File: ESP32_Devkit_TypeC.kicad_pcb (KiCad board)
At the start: 2 copper layers, 25.3 x 48.2 mm, 43 parts, among them J1 USB_C_Receptacle_USB2.0, J2 Conn_01x19, J3 Conn_01x19, Q1 SS8050, Q2 SS8050, SW1 EN, SW2 BOOT, U1 MP2451, U2 CH340G, U3 ESP32-PICO-D4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

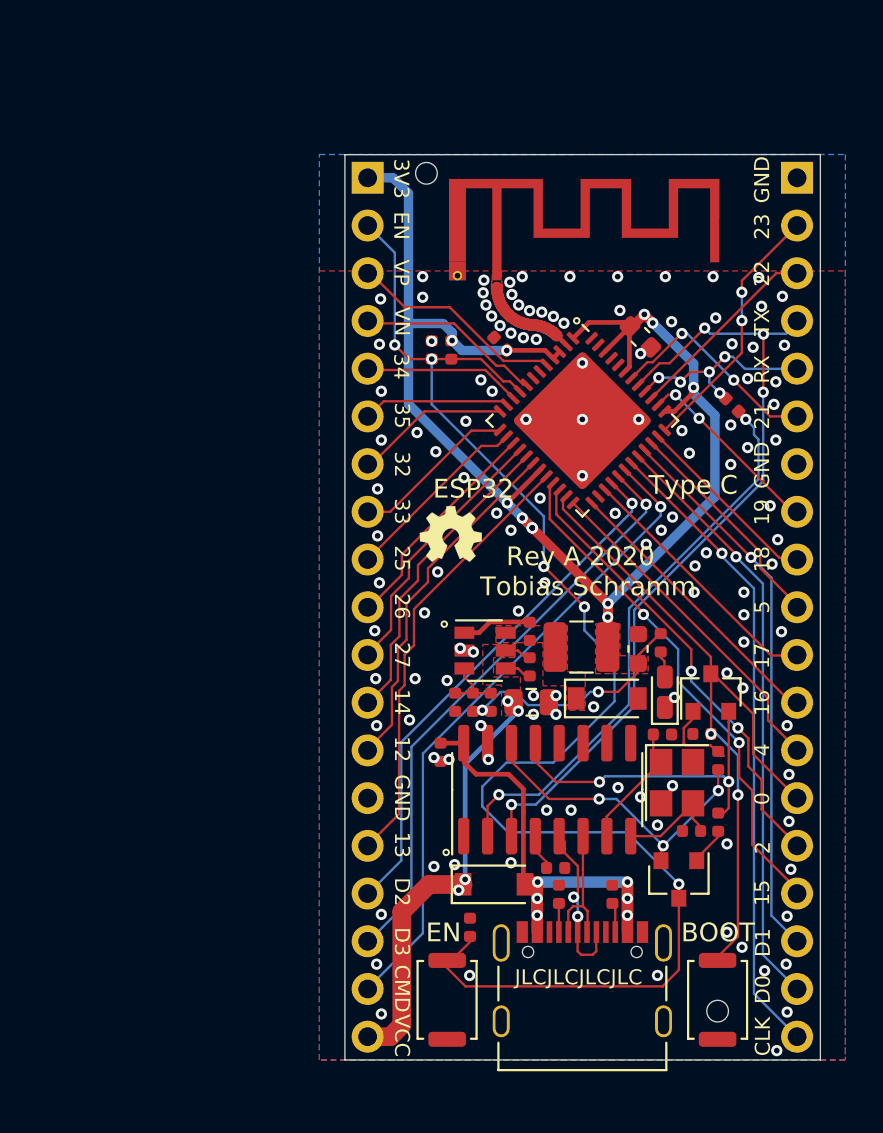
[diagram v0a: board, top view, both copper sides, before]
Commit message: Use ESP32 Pico D4 footprint
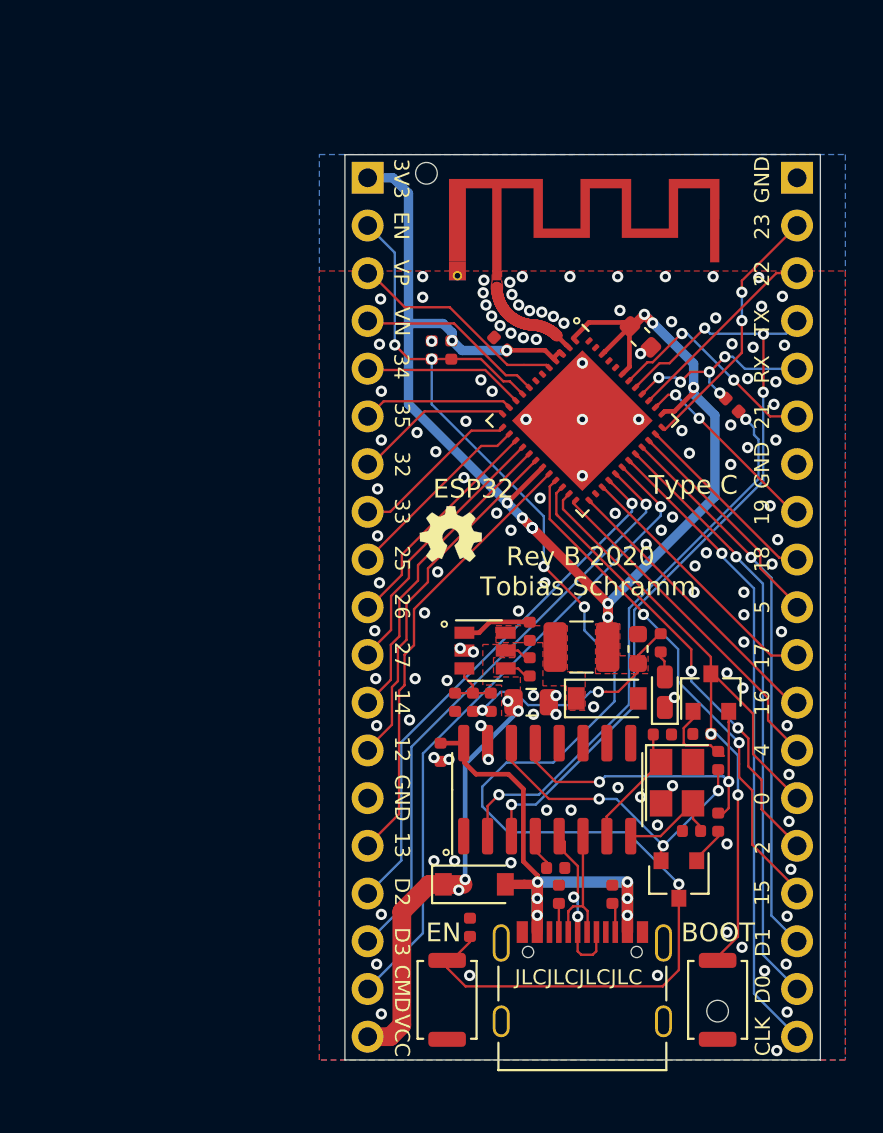
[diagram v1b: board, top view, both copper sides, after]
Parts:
- U3: footprint Package_DFN_QFN:QFN-48-1EP_7x7mm_P0.5mm_EP5.3x5.3mm -> Package_ESP32:ESP32-Pico-D4
- moved D1 1.05 mm to (94.2, 114.8)
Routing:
- net VBUS: track 25.2 -> 26.8 mm
- net +3V3: track 91.7 -> 92.9 mm
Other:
- board text added: "Rev B 2020"
- board text removed: "Rev A 2020"

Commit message: Rev B
Changes from Rev A:
 - Fix ESP32 Pico D4 footprint, now LGA
 - Add couple capacitor from EN to IO0
 - Add protection resistors to EN and IO0
 - Move VBUS diode for easier USB Type C jack assembly
 - Small routing optimizations
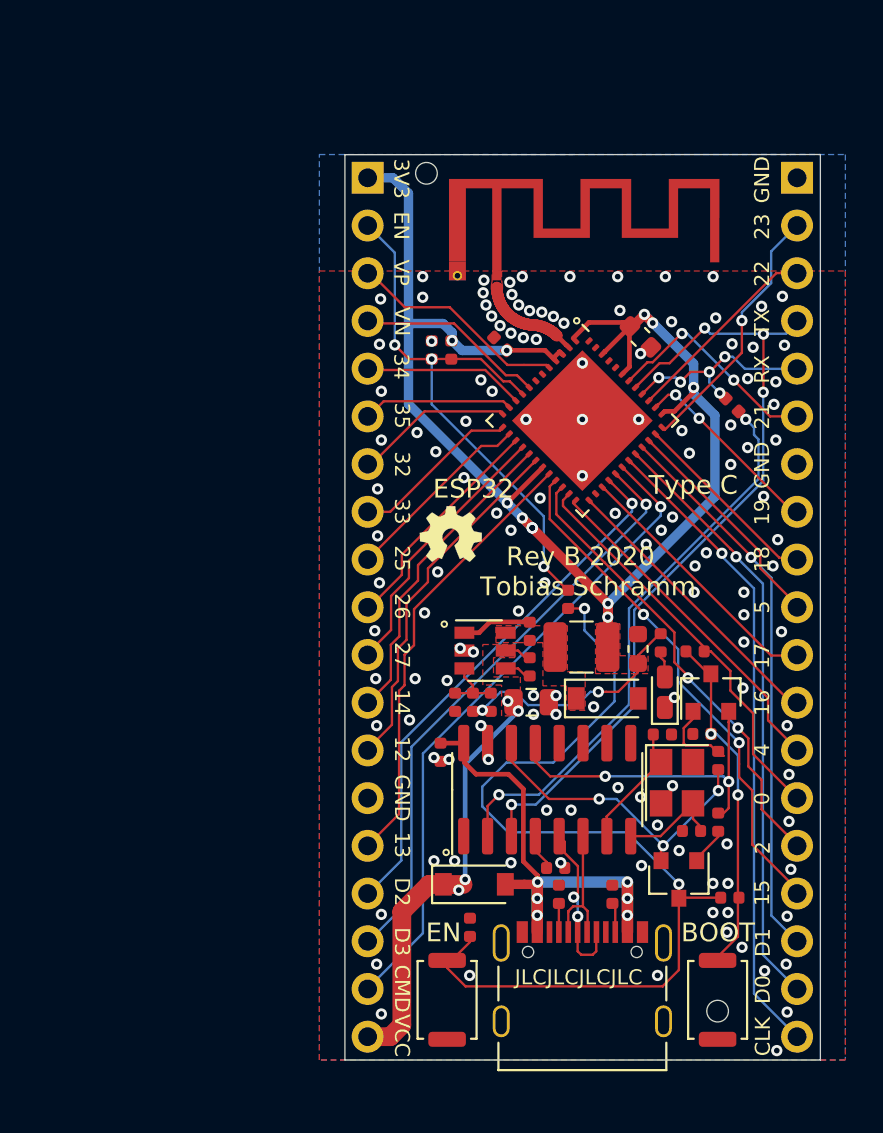
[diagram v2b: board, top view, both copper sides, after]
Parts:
- added C6: 100 nF, Capacitor_SMD:C_0402_1005Metric, F.Cu at (107.8, 115.5)
- added R11: 330 R, Resistor_SMD:R_0402_1005Metric, F.Cu at (99.2, 99.6)
- added R12: 330 R, Resistor_SMD:R_0402_1005Metric, F.Cu at (106.0, 102.3)
- C1: value 100 nF -> 10 nF
- C8: value 10 uF -> 22 uF
- C9: value 33 pF -> DNP
- L1: value 2.2 uH -> 4.7 uH
- R1: value 10 kR -> 100 kR
- R5: value 120 kR -> 49.9kR
- R6: value 39 kR -> 15 kR
- U1: value MP2451 -> MP2359
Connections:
- C10 pad 2: /EN -> Net-(C10-Pad2)
- C11 pad 2: /IO0 -> Net-(C11-Pad2)
- Q1 pad 3: /EN -> Net-(C10-Pad2)
- Q2 pad 3: /IO0 -> Net-(C11-Pad2)
- SW1 pad 1: /EN -> Net-(C10-Pad2)
- SW2 pad 1: /IO0 -> Net-(C11-Pad2)
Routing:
- net Net-(C10-Pad2): track 0.00 -> 50.9 mm, vias 0 -> 2
- net /EN: track 79.1 -> 30.0 mm, vias 5 -> 3
- net Net-(C11-Pad2): track 0.00 -> 18.4 mm, vias 0 -> 2
- net /IO0: track 37.9 -> 21.6 mm, vias 2 -> 0
- net /IO23: vias 2 -> 1
- net GND: vias 127 -> 132

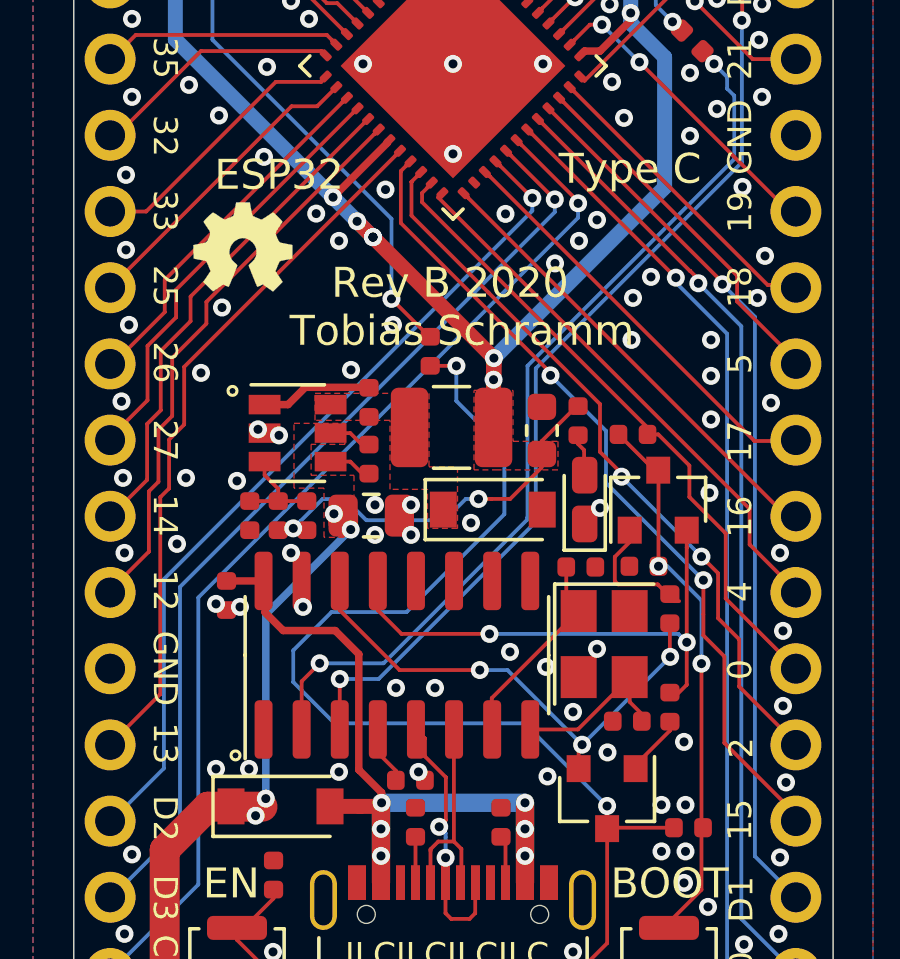
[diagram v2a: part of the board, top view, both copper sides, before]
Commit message: Fix step down GND routing
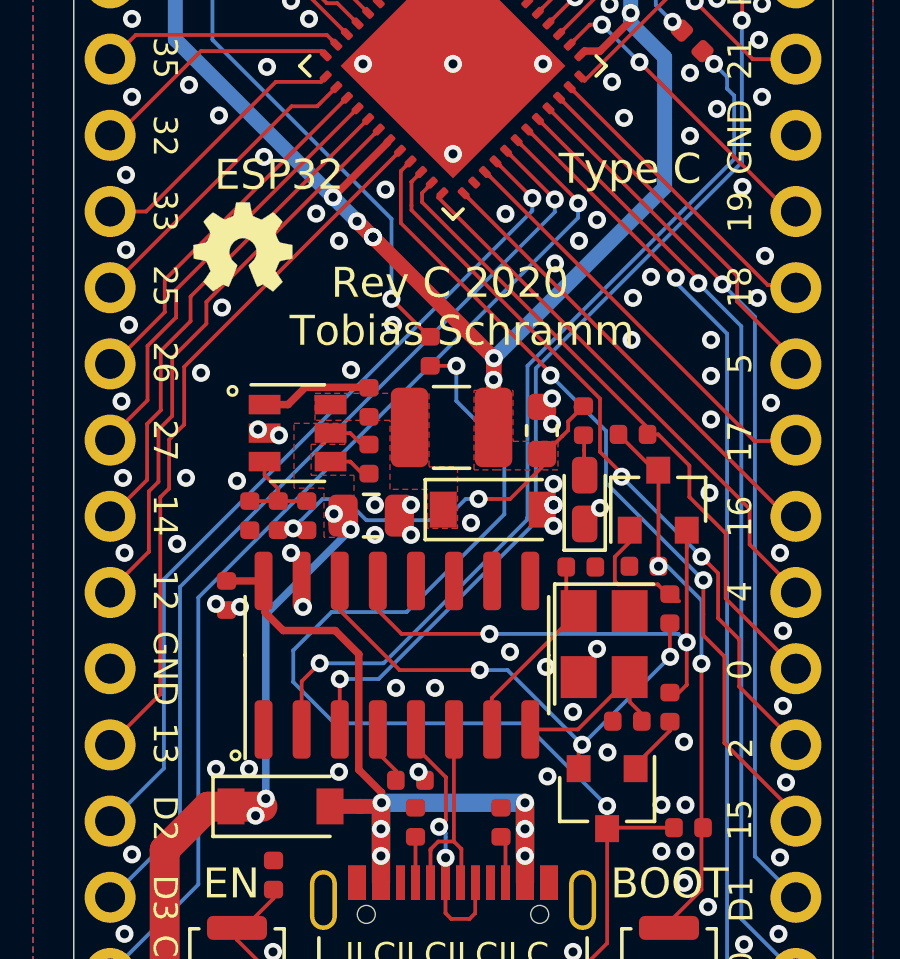
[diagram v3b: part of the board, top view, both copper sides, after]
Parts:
- moved R9 0.18 mm to (104.3, 101.9)
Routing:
- net GND: vias 132 -> 138
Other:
- board text added: "Rev C 2020"
- board text removed: "Rev B 2020"

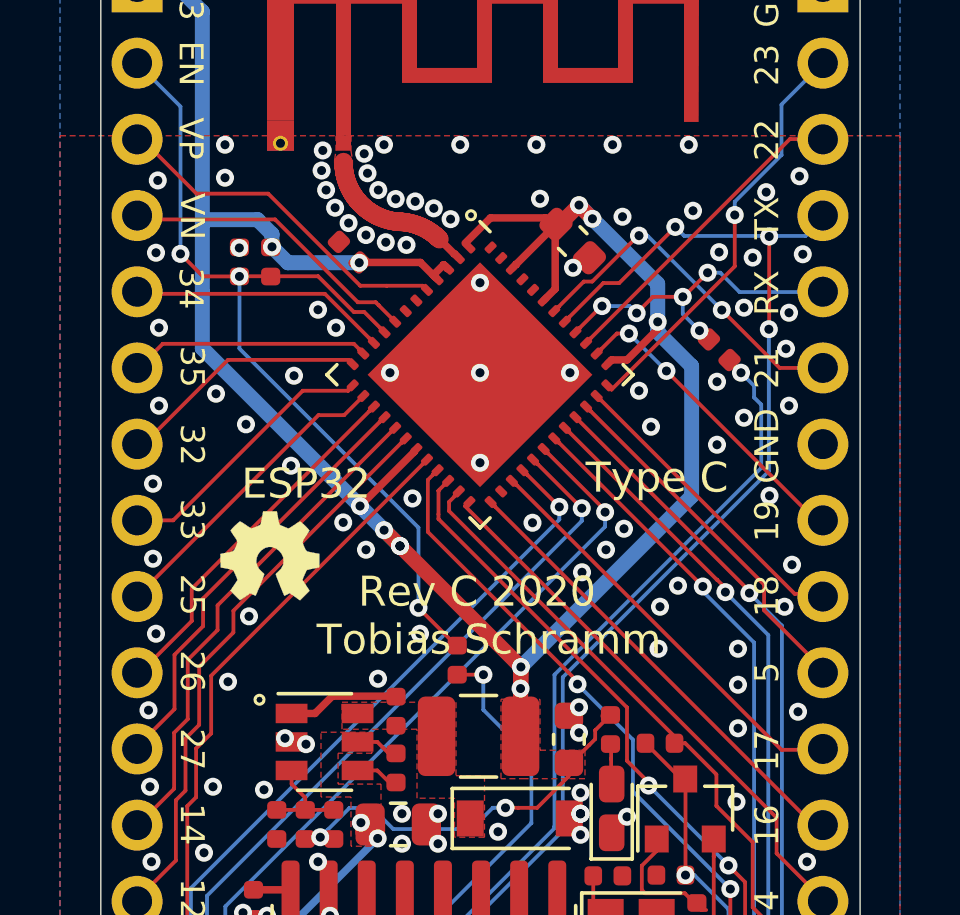
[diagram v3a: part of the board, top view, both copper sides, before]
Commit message: Rev C
Changes from Rev B:

* Add more bypassing to ESP32 Pico D4
* Reduce ground loop area of step-down significantly
* Fix ugly routing of USB D+
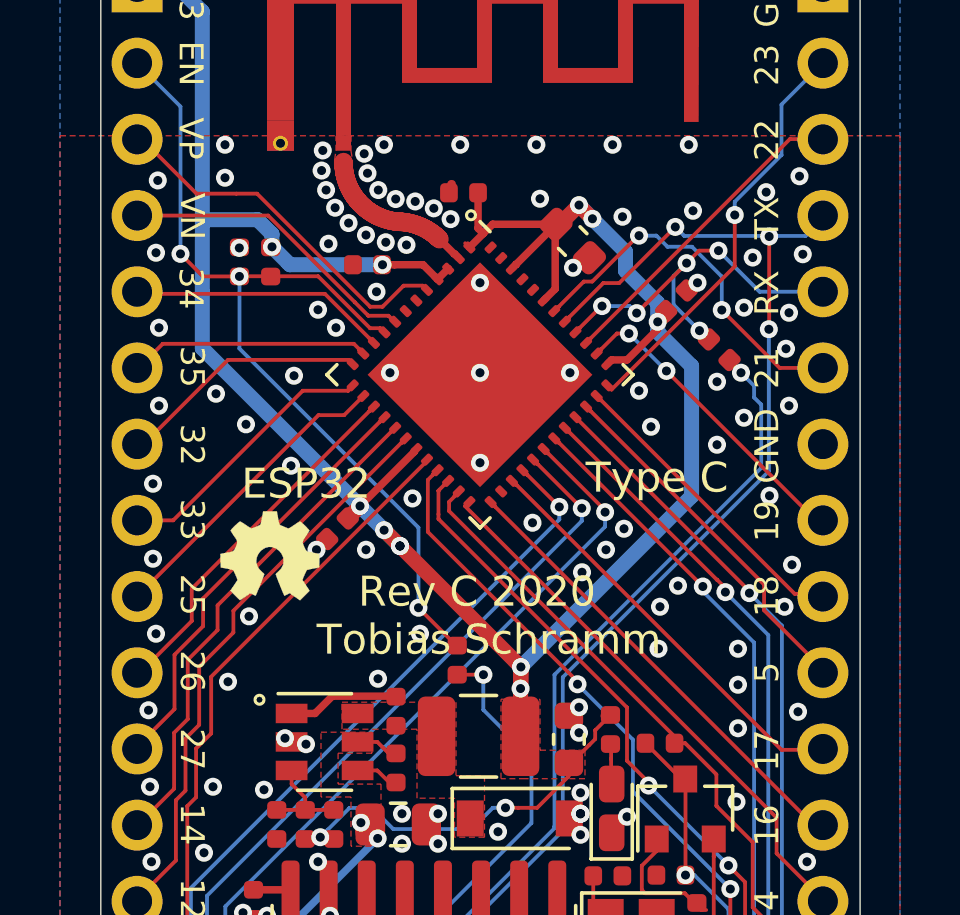
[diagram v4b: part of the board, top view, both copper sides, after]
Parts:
- added C15: 100 nF, Capacitor_SMD:C_0402_1005Metric, F.Cu at (99.5, 84.0)
- added C16: 100 nF, Capacitor_SMD:C_0402_1005Metric, F.Cu at (95.2, 95.2)
- added C17: 100 nF, Capacitor_SMD:C_0402_1005Metric, F.Cu at (106.5, 87.6)
- moved C14 0.74 mm to (96.2, 86.4), turned to 0 degrees
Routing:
- net /RXD: track 11.3 -> 13.3 mm
- net +3V3: track 93.2 -> 95.0 mm
- net /IO21: track 11.8 -> 12.7 mm
- net /VP: track 11.6 -> 12.2 mm
- net GND: track 0.00 -> 0.04 mm, vias 138 -> 140

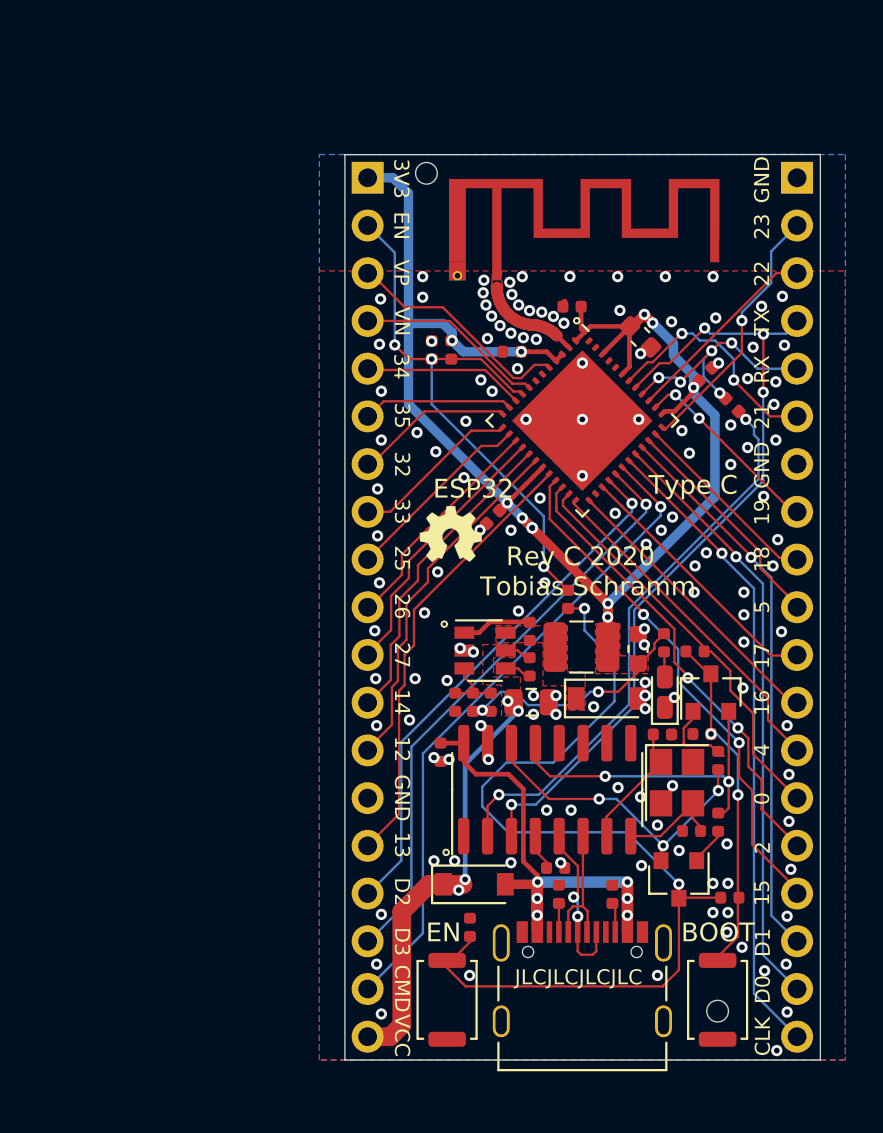
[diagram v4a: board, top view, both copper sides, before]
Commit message: Rev D
Most importantly this revision improves reset/bootloader behaviour
by increasing the RC time constant of the reset RC network considerably.
(~50ms vs 1ms). This makes programming more reliable on machines with
high DTR/RTS setting delays or when working with USB over IP solutions.

Full list of changes:
* Improve reset/flash behaviour
* Eliminate 10k resistors
* Reduce brightness of power led
* Remove Corona warning
* Remove groundplane below antenna
* Eliminate cap from EN to IO0, causes boot issues
* Add input diode shorting jumper
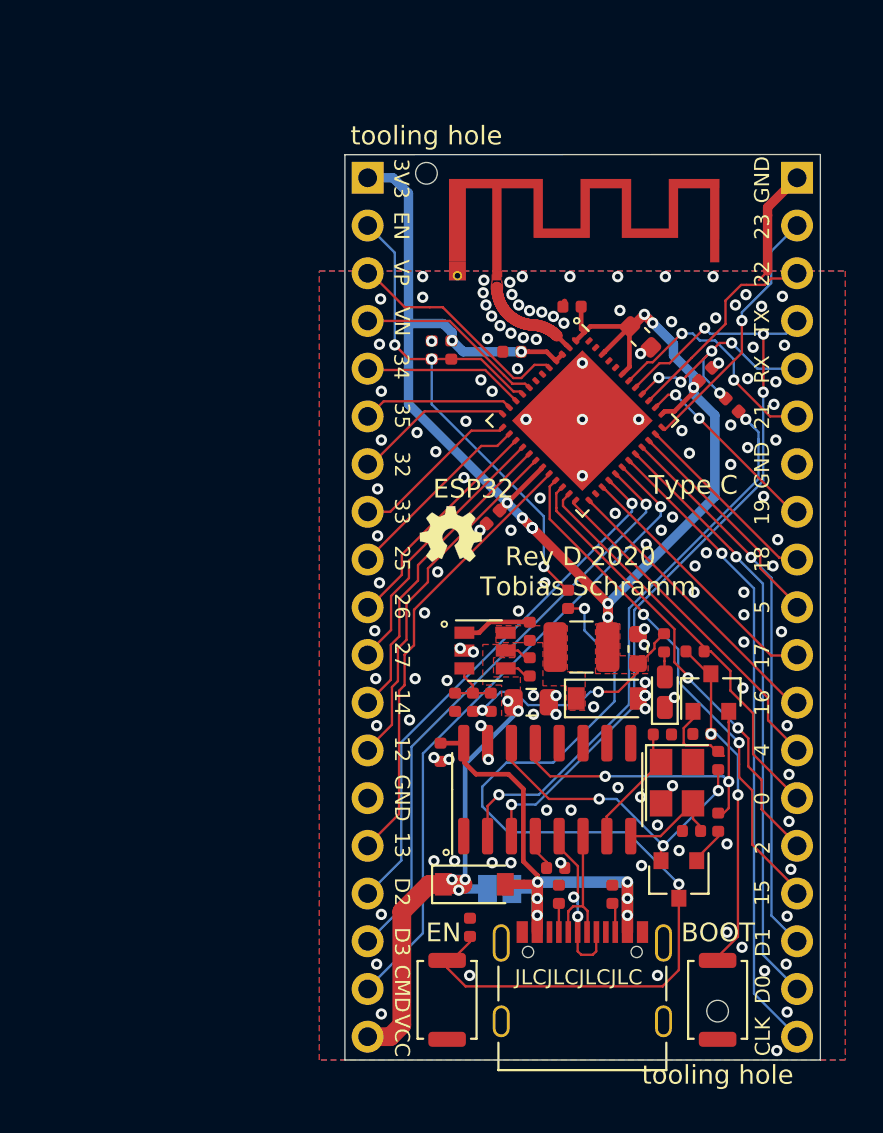
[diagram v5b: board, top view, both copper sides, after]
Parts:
- removed the C6 at (107.8, 115.5)
- removed I1: Icon, Signs:Danger_RF_Corona
- added JP1: SolderJumper_2_Open, Jumper:SolderJumper-2_P1.3mm_Open_Pad1.0x1.5mm, B.Cu at (95.6, 115.0)
- C10: value 100 nF -> DNP
- C12: value 100 nF -> 1uF
- R10: value 10 kR -> 100 kR
- R7, R8: value 10 kR -> 5.1kR
- R9: value 1 kR -> 5.1kR
- Y1: value Crystal_GND24 -> 12MHz
- renumbered C17 to C6
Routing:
- net GND: track 0.04 -> 6.74 mm, vias 140 -> 139
- net VCC: track 25.3 -> 28.2 mm, vias 4 -> 5
- net Net-(C10-Pad2): track 50.9 -> 48.7 mm
- net VBUS: track 26.8 -> 28.2 mm
- net /IO22: track 10.7 -> 11.6 mm
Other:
- board text added: "Rev D 2020"
- board text added: "short diode"
- board text removed: "Rev C 2020"
